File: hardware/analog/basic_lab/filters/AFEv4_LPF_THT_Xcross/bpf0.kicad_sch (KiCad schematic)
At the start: 9 parts, among them J3 Connector_Generic_Conn_01x02, J4 Connector_Generic_Conn_01x02

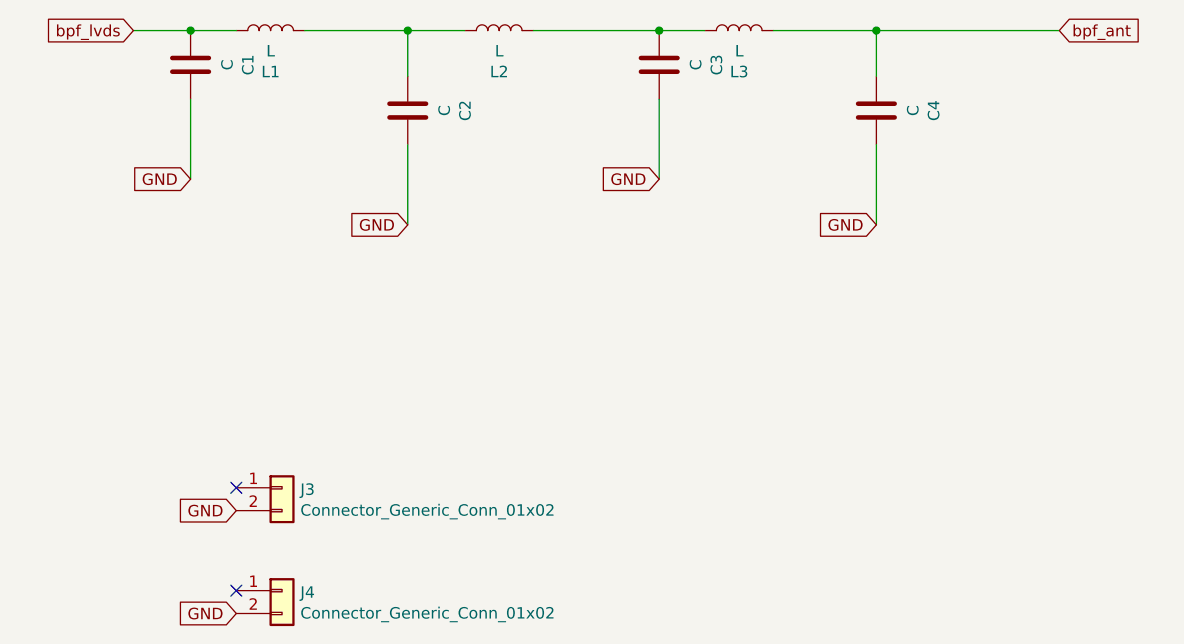
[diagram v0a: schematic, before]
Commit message: started PCB THT LPF
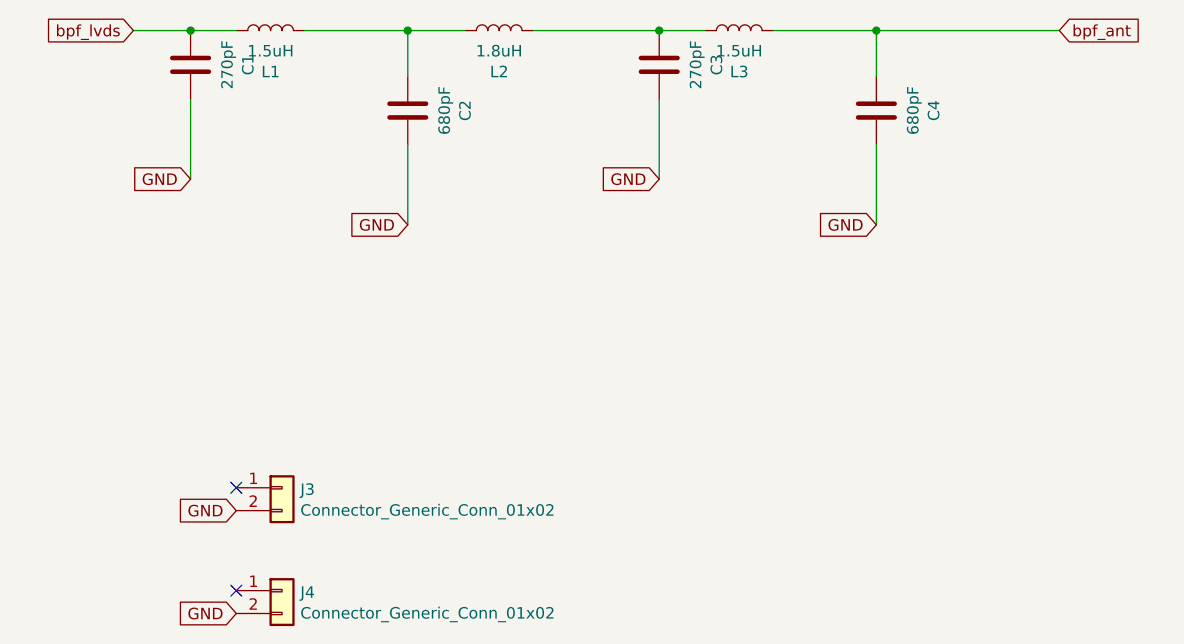
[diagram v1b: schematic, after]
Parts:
- C1, C3: value C -> 270pF; footprint Capacitor_SMD:C_1206_3216Metric -> Capacitor_THT:CP_Radial_D8.0mm_P5.00mm
- C2, C4: value C -> 680pF; footprint Capacitor_SMD:C_1206_3216Metric -> Capacitor_THT:CP_Radial_D8.0mm_P5.00mm
- L1, L3: value L -> 1.5uH; footprint Inductor_SMD:L_1206_3216Metric -> Inductor_THT:L_Axial_L9.5mm_D4.0mm_P12.70mm_Horizontal_Fastron_SMCC
- L2: value L -> 1.8uH; footprint Inductor_SMD:L_1206_3216Metric -> Inductor_THT:L_Axial_L9.5mm_D4.0mm_P12.70mm_Horizontal_Fastron_SMCC
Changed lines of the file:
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@@
     (in_bom yes) (on_board yes)
     (property "Reference" "C1" (id 0) (at 67.3608 72.39 90))
-    (property "Value" "C" (id 1) (at 65.0494 72.39 90))
-    (property "Footprint" "Capacitor_SMD:C_1206_3216Metric" (id 2) (at 59.9948 68.58 0)
+    (property "Value" "270pF" (id 1) (at 65.0494 72.39 90))
+    (property "Footprint" "Capacitor_THT:CP_Radial_D8.0mm_P5.00mm" (id 2) (at 59.9948 68.58 0)
       (effects (font (size 1.27 1.27)) hide)
     )
@@
     (in_bom yes) (on_board yes)
     (property "Reference" "L2" (id 0) (at 95.25 73.1774 90))
-    (property "Value" "L" (id 1) (at 95.25 70.866 90))
-    (property "Footprint" "Inductor_SMD:L_1206_3216Metric" (id 2) (at 95.25 68.58 0)
+    (property "Value" "1.8uH" (id 1) (at 95.25 70.866 90))
+    (property "Footprint" "Inductor_THT:L_Axial_L9.5mm_D4.0mm_P12.70mm_Horizontal_Fastron_SMCC" (id 2) (at 95.25 68.58 0)
       (effects (font (size 1.27 1.27)) hide)
     )
@@
     (in_bom yes) (on_board yes)
     (property "Reference" "C2" (id 0) (at 91.4908 77.47 90))
-    (property "Value" "C" (id 1) (at 89.1794 77.47 90))
-    (property "Footprint" "Capacitor_SMD:C_1206_3216Metric" (id 2) (at 84.1248 73.66 0)
+    (property "Value" "680pF" (id 1) (at 89.1794 77.47 90))
+    (property "Footprint" "Capacitor_THT:CP_Radial_D8.0mm_P5.00mm" (id 2) (at 84.1248 73.66 0)
       (effects (font (size 1.27 1.27)) hide)
     )
@@
     (in_bom yes) (on_board yes)
     (property "Reference" "L1" (id 0) (at 69.85 73.1774 90))
-    (property "Value" "L" (id 1) (at 69.85 70.866 90))
-    (property "Footprint" "Inductor_SMD:L_1206_3216Metric" (id 2) (at 69.85 68.58 0)
+    (property "Value" "1.5uH" (id 1) (at 69.85 70.866 90))
+    (property "Footprint" "Inductor_THT:L_Axial_L9.5mm_D4.0mm_P12.70mm_Horizontal_Fastron_SMCC" (id 2) (at 69.85 68.58 0)
       (effects (font (size 1.27 1.27)) hide)
     )
@@
     (in_bom yes) (on_board yes)
     (property "Reference" "C3" (id 0) (at 119.4308 72.39 90))
-    (property "Value" "C" (id 1) (at 117.1194 72.39 90))
-    (property "Footprint" "Capacitor_SMD:C_1206_3216Metric" (id 2) (at 112.0648 68.58 0)
+    (property "Value" "270pF" (id 1) (at 117.1194 72.39 90))
+    (property "Footprint" "Capacitor_THT:CP_Radial_D8.0mm_P5.00mm" (id 2) (at 112.0648 68.58 0)
       (effects (font (size 1.27 1.27)) hide)
     )
@@
     (in_bom yes) (on_board yes)
     (property "Reference" "L3" (id 0) (at 121.92 73.1774 90))
-    (property "Value" "L" (id 1) (at 121.92 70.866 90))
-    (property "Footprint" "Inductor_SMD:L_1206_3216Metric" (id 2) (at 121.92 68.58 0)
+    (property "Value" "1.5uH" (id 1) (at 121.92 70.866 90))
+    (property "Footprint" "Inductor_THT:L_Axial_L9.5mm_D4.0mm_P12.70mm_Horizontal_Fastron_SMCC" (id 2) (at 121.92 68.58 0)
       (effects (font (size 1.27 1.27)) hide)
     )
@@
     (in_bom yes) (on_board yes)
     (property "Reference" "C4" (id 0) (at 143.5608 77.47 90))
-    (property "Value" "C" (id 1) (at 141.2494 77.47 90))
-    (property "Footprint" "Capacitor_SMD:C_1206_3216Metric" (id 2) (at 136.1948 73.66 0)
+    (property "Value" "680pF" (id 1) (at 141.2494 77.47 90))
+    (property "Footprint" "Capacitor_THT:CP_Radial_D8.0mm_P5.00mm" (id 2) (at 136.1948 73.66 0)
       (effects (font (size 1.27 1.27)) hide)
     )
